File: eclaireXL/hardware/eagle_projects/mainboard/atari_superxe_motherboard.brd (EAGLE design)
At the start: 150 x 100 mm, 147 parts, among them U1 EPCS

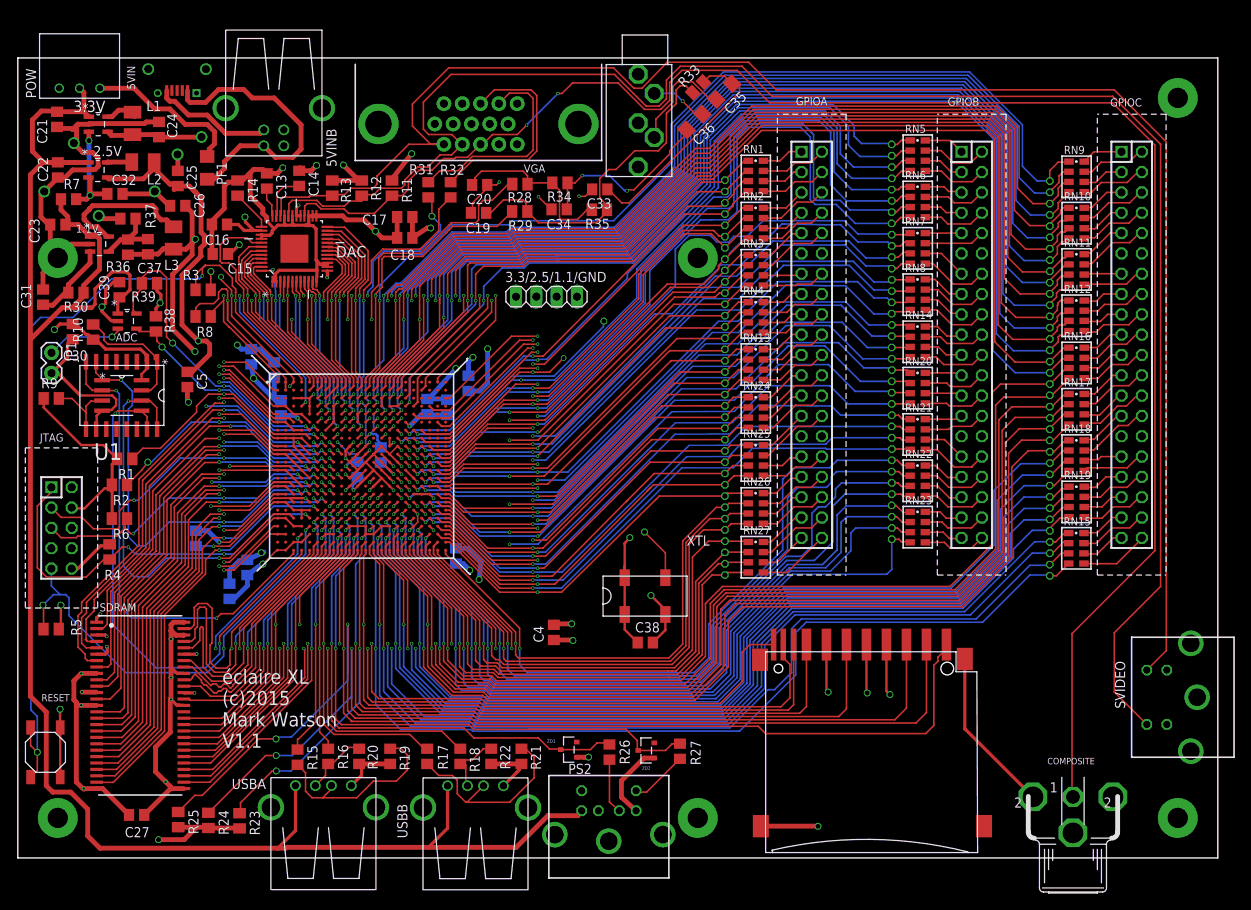
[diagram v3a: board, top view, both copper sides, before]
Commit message: Moved video ports to the back (painful!!). Added rocker switch on left for power.
git-svn-id: http://www.64kib.com/atarixlfpga_svn/trunk/atari_800xl@424 d6161ac3-aae1-4d52-9b05-ea9ac36b53d3
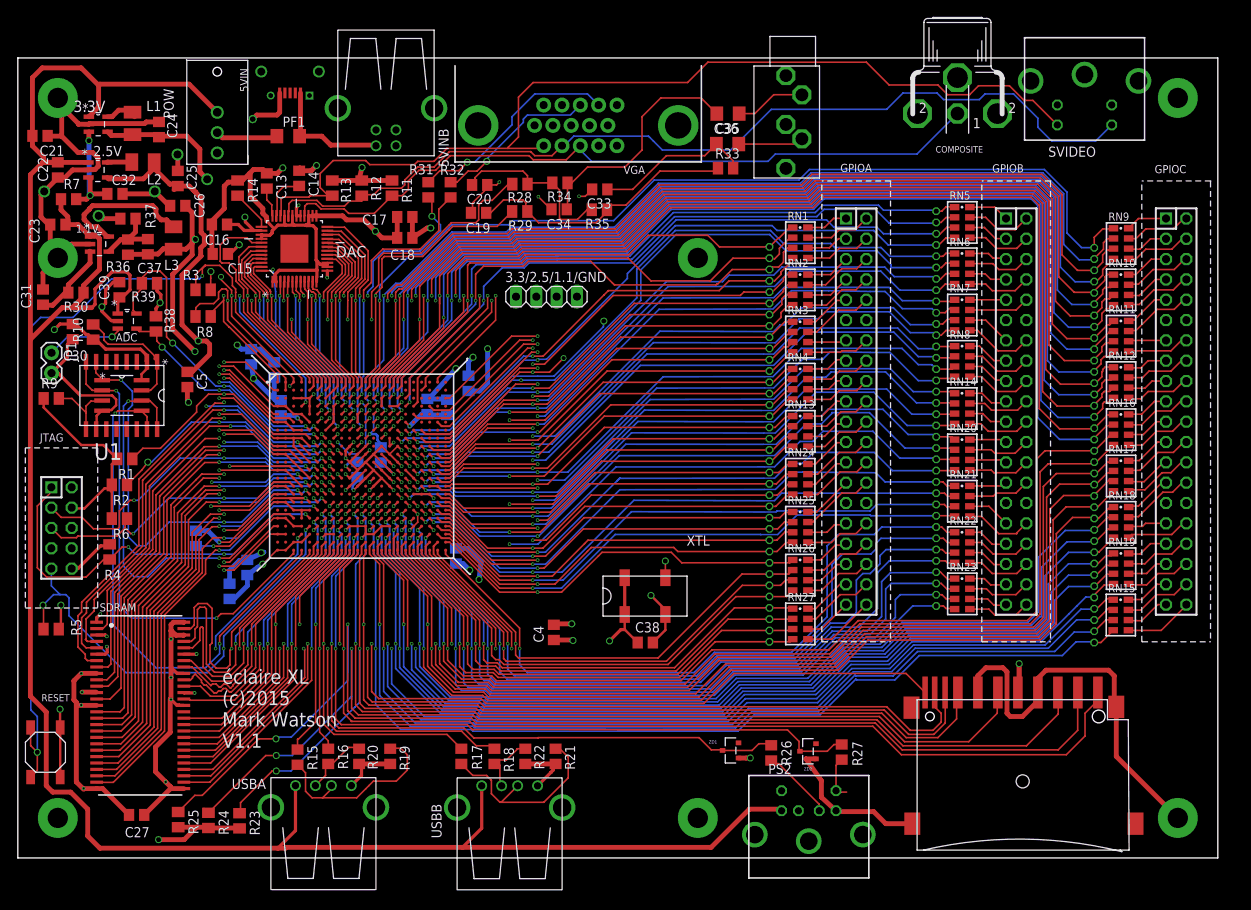
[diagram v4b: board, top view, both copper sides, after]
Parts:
- added H7: MOUNT-PAD-ROUND2.5, holes:2,5-PAD
- POW: value 450302014072 -> 450302014072ROCKER; device Eagle_Wuerth_Elektronik_Switch_rev15b:450302014072 -> Eagle_Wuerth_Elektronik_Switch_rev15b:ROCKER_VERT_SPDT
- U$2: value SDMMC06132 -> SDMMCHALFHEIGHT; device adafruit:06132 -> adafruit:HALFHEIGHTSD
- moved COMPOSITE 86.6 mm to (117.5, 93.0), turned to 0 degrees
- moved SVIDEO 84.7 mm to (133.3, 102.6), turned to 180 degrees
- moved PS2 25.0 mm to (98.9, -2.60)
- moved U$2 24.9 mm to (125.6, 9.62)
- moved R26 20.2 mm to (94.2, 13.1)
- moved R27 20.2 mm to (103.0, 13.2)
- moved ZD1 20.2 mm to (89.1, 13.4)
- moved ZD2 20.2 mm to (98.8, 13.3)
- moved AUDIO 18.5 mm to (97.9, 93.2)
- moved POW 17.4 mm to (24.9, 93.7)
- moved 5VIN 14.1 mm to (34.0, 98.3)
- moved 5VINB 14.0 mm to (46.0, 91.0)
- moved VGA 12.5 mm to (70.1, 96.6)
- moved PF1 10.9 mm to (33.8, 90.2), turned to 180 degrees
- moved R33 10.7 mm to (88.5, 86.2), turned to 180 degrees
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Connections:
- net 5V0: now also POW.P$1; no longer POW.1
- net GND: now also H7.B2,8
- net N$139: now also POW.P$2; no longer POW.3
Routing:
- net N$143: track 210.2 -> 91.8 mm, vias 2 -> 0
- net N$14: track 217.4 -> 119.2 mm
- net N$13: track 203.3 -> 122.2 mm
- net 5V0: track 431.0 -> 480.9 mm
- net N$2: track 36.2 -> 15.5 mm
- net PS2DAT: track 61.3 -> 81.6 mm
- net PS2CLK: track 73.3 -> 93.6 mm
- net GPIOB7: track 96.2 -> 77.8 mm
- net GPIOB6: track 91.9 -> 74.2 mm
- net SD_DETECT: track 85.9 -> 103.0 mm
- net SD_CS: track 151.3 -> 168.3 mm
- net SD_DAT1: track 80.9 -> 97.7 mm
- net SD_WRITEPROTECT: track 79.3 -> 95.5 mm
- net SD_MISO: track 114.2 -> 130.4 mm
- net SD_MOSI: track 136.5 -> 152.6 mm
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
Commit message: HDMI port
git-svn-id: http://www.64kib.com/atarixlfpga_svn/trunk/atari_800xl@436 d6161ac3-aae1-4d52-9b05-ea9ac36b53d3
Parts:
- added RN28, RN29: 270, resistor-array:743-8
- added X1: HDMI, raspberrypi_cm:HDMI
- POW: value 450302014072ROCKER -> 450302014072ROCKER2; device Eagle_Wuerth_Elektronik_Switch_rev15b:ROCKER_VERT_SPDT -> Eagle_Wuerth_Elektronik_Switch_rev15b:ROCKER_VERT_SPDT2
- moved C20 73.4 mm to (131.0, 87.4), turned to 0 degrees
- moved C34 70.1 mm to (137.8, 83.6)
- moved C19 68.4 mm to (125.7, 87.4), turned to 0 degrees
- moved R34 65.2 mm to (133.0, 83.6)
- moved C33 65.1 mm to (137.8, 81.0)
- moved C35 57.2 mm to (145.8, 86.2)
- moved C36 57.1 mm to (145.8, 90.0)
- moved R28 52.4 mm to (115.1, 87.6)
- moved R35 47.9 mm to (120.1, 87.5)
- moved R29 47.1 mm to (109.6, 85.7)
- moved R33 44.9 mm to (133.1, 80.9)
- moved AUDIO 41.9 mm to (139.8, 93.4)
- moved R31 23.5 mm to (74.8, 83.3), turned to 0 degrees
- moved R32 20.9 mm to (74.8, 80.8), turned to 0 degrees
- moved VGA 18.2 mm to (88.1, 94.7)
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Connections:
- new net N$134: RN28.8, X1.1
- new net N$144: RN28.7, X1.3
- new net N$146: RN28.6, X1.4
- new net N$147: RN28.5, X1.6
- new net N$148: RN29.8, X1.7
- new net N$149: RN29.7, X1.9
- new net N$150: RN29.6, X1.10
- new net N$151: RN29.5, X1.12
- net 5V0: now also POW.P$3, X1.18; no longer POW.P$1
- net GND: now also X1.11, X1.17, X1.2, X1.5, X1.8, X1.P$1, X1.P$2, X1.P$3, X1.P$4
- net VGA_B1: now also RN29.2
- net VGA_B4: now also RN29.1
- net VGA_B5: now also RN29.4
- net VGA_B6: now also RN29.3
- net VGA_R0: now also RN28.1
- net VGA_R1: now also RN28.2
- net VGA_R3: now also RN28.4
- net VGA_R4: now also RN28.3
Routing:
- net AUDIO_LEFT: track 46.6 -> 99.6 mm
- net AUDIO_RIGHT: track 35.0 -> 83.8 mm
- net VGA_R1: track 24.7 -> 59.9 mm, vias 1 -> 3
- net VGA_R4: track 23.4 -> 58.5 mm, vias 2 -> 4
- net VGA_R3: track 25.2 -> 60.2 mm, vias 2 -> 4
- net VGA_R0: track 28.1 -> 57.5 mm, vias 1 -> 3
- net VGA_B5: track 27.4 -> 55.5 mm, vias 2 -> 4
- net VGA_B1: track 26.2 -> 53.6 mm, vias 2 -> 4
- net VGA_B6: track 30.3 -> 56.8 mm, vias 2 -> 4
- net VGA_B4: track 25.8 -> 51.2 mm, vias 2 -> 4
- net N$13: track 122.2 -> 102.9 mm, vias 0 -> 1
- net VSYNC: track 38.1 -> 56.7 mm
- net 5V0: track 480.9 -> 499.4 mm, vias 0 -> 3
- net HSYNC: track 32.6 -> 50.1 mm
- net GND: track 871.9 -> 887.6 mm, vias 85 -> 83
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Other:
- board text added: "éclaire XL (c)2016 Mark Watson V1.2"
- board text removed: "éclaire XL (c)2015 Mark Watson V1.1"

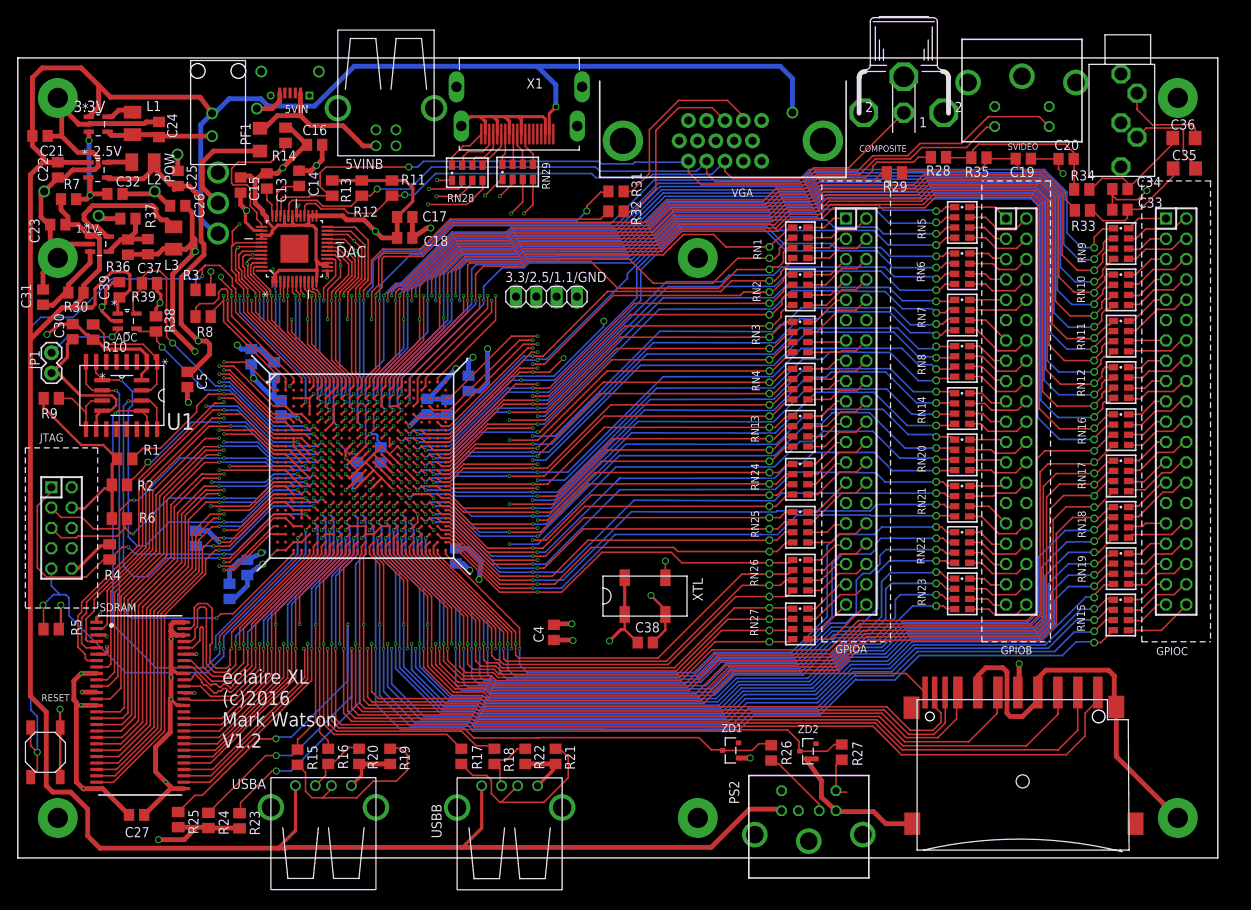
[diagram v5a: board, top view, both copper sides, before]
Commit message: Update from Panos (many thanks). Adjusted labels, tidied endings where nets meet pins
git-svn-id: http://www.64kib.com/atarixlfpga_svn/trunk/atari_800xl@472 d6161ac3-aae1-4d52-9b05-ea9ac36b53d3
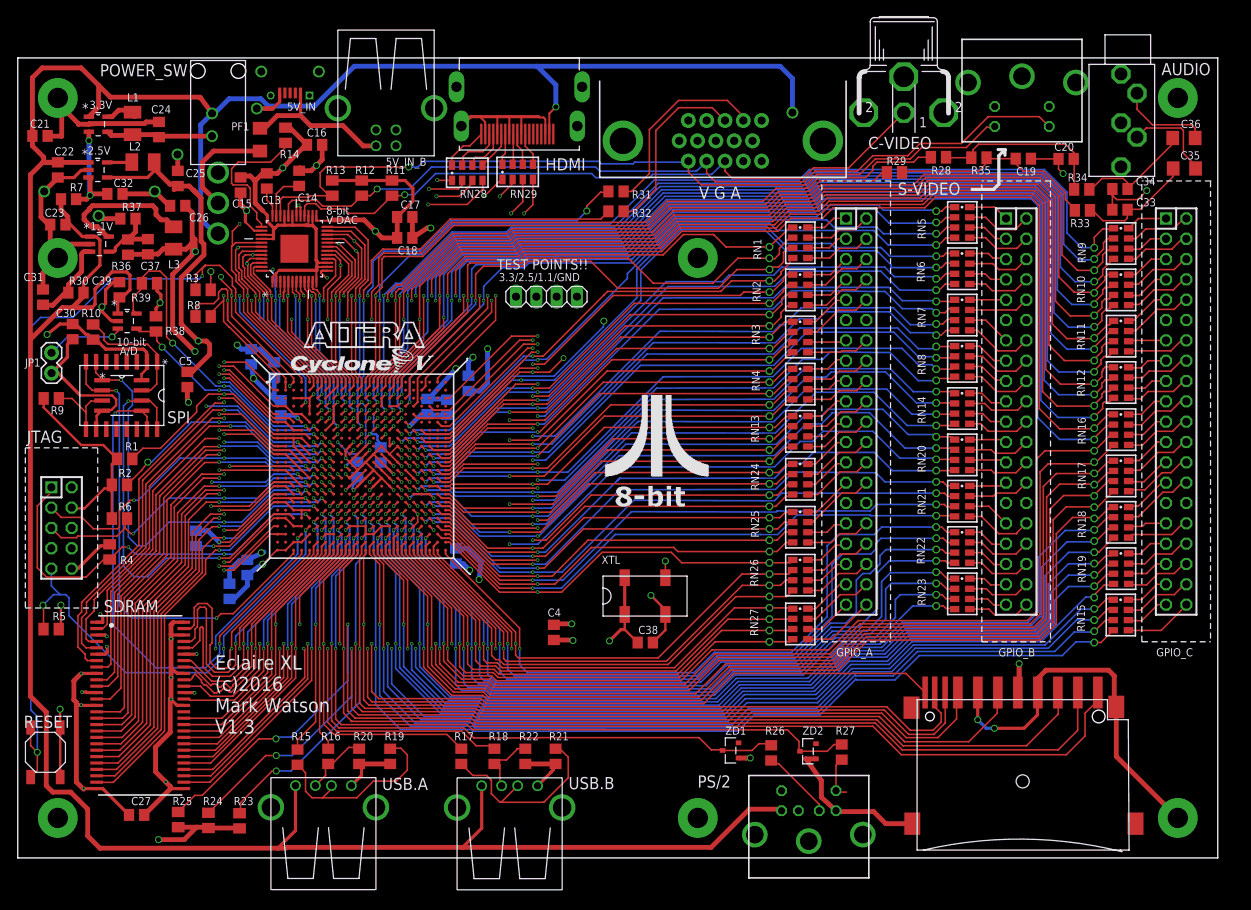
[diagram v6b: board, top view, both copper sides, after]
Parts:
- AUDIO: device stereoaudiojack:AUDIO-JACK-CUI-353X -> LIBstereoaudiojack:AUDIO-JACK-CUI-353X
- renumbered 5VIN to 5V_IN, 5VINB to 5V_IN_B, COMPOSITE to C-VIDEO, DAC to VIDEODACSA, GPIOA to GPIO_A, GPIOB to GPIO_B, GPIOC to GPIO_C, POW to POWER_SW, PS2 to PS/2, SVIDEO to S-VIDEO, U1 to SPI, USBA to USB.A, USBB to USB.B, X1 to HDMI
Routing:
- net GND: track 887.6 -> 880.3 mm, vias 83 -> 85
- net 3V3: track 485.3 -> 486.5 mm
- net VGA_B5: track 55.5 -> 54.9 mm
- net VGA_B3: track 22.4 -> 21.8 mm
- net VGA_B4: track 51.2 -> 50.6 mm
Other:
- board text added: "10-bit A/D"
- board text added: "8-bit V DAC"
- board text added: "AUDIO"
- board text added: "Eclaire XL (c)2016 Mark Watson V1.3"
- board text added: "TEST POINTS!!"
- board text added: "V G A"
- board text removed: "éclaire XL (c)2016 Mark Watson V1.2"
